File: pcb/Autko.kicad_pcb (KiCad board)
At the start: 2 copper layers, 130 parts, among them J1 PDI, M1 LEFT, M2 RIGHT, Q1 Si4368DY, Q2 BC817, SW2 START, SW3 STOP, U1 LTC3872, U10 CNY70, U11 CNY70, U12 TB6612FNG, U13 RN4678, U2 TLV1117-33, U3 ATxmega16A4U-A, U5 CNY70, U6 CNY70, U7 CNY70, U8 CNY70, U9 CNY70, Y1 8MHz

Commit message: [pcb] Initial layout
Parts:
- removed U13: RN4678, Autko:RN4678
- added REF**: Pololu_ball_caster, Autko:Pololu_ball_caster, F.Cu at (189.7, 48.1)
- added SW1: POWER, Autko:Knitter-Switch_MSS_3112_D, F.Cu at (65.0, 117.5)
- added U4: CNY70, OptoDevice:Vishay_CNY70, F.Cu at (70.6, -19.8)
- R15, R16, R17, R18, R19, R20, R21, R22: value 10kR -> ???R
- U11: value CNY70 -> TB6612FNG; footprint OptoDevice:Vishay_CNY70 -> Package_SO:SSOP-24_5.3x8.2mm_P0.65mm
- U12: value TB6612FNG -> RN4678; footprint Package_SO:SSOP-24_5.3x8.2mm_P0.65mm -> Autko:RN4678
- moved TP14 132.6 mm to (56.0, -6.50)
- moved U11 129.6 mm to (128.5, 176.0), turned to 90 degrees
- moved Y1 119.6 mm to (122.5, 38.5), turned to 180 degrees
- moved R37 119.5 mm to (60.0, -6.50)
- moved Q2 116.7 mm to (65.0, -6.50)
- moved SW2 116.6 mm to (52.8, 84.2)
- moved SW3 115.6 mm to (52.8, 95.2)
- moved C19 114.8 mm to (120.0, 44.5), turned to 180 degrees
- moved M1 114.4 mm to (39.5, 140.5), turned to 90 degrees
- moved C21 109.6 mm to (128.5, 169.5)
- moved TP7 108.7 mm to (72.0, -11.5)
- moved R23 108.3 mm to (70.0, -25.5)
- moved C17 108.0 mm to (64.1, 88.5)
- moved C22 107.9 mm to (122.5, 173.5), turned to -90 degrees
- moved M2 106.6 mm to (159.5, 140.5), turned to -90 degrees
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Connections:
- D10 pad 2: Net-(D10-A) -> /Microcontroller/LED7
- D11 pad 2: Net-(D11-A) -> /Microcontroller/LED8
- D4 pad 2: Net-(D4-A) -> /Microcontroller/LED1
- D5 pad 2: Net-(D5-A) -> /Microcontroller/LED2
- D6 pad 2: Net-(D6-A) -> /Microcontroller/LED3
- D7 pad 2: Net-(D7-A) -> /Microcontroller/LED4
- D8 pad 2: Net-(D8-A) -> /Microcontroller/LED5
- D9 pad 2: Net-(D9-A) -> /Microcontroller/LED6
- R13 pad 2: Net-(U3-AREFA/PA0) -> Net-(U3-PA7)
- R14 pad 1: Net-(U3-AREFA/PA0) -> Net-(U3-PA7)
- R15 pad 1: +3.3V -> Net-(D4-K)
- R15 pad 2: Net-(D4-A) -> GND
- R16 pad 1: +3.3V -> Net-(D5-K)
- R16 pad 2: Net-(D5-A) -> GND
- R17 pad 1: +3.3V -> Net-(D6-K)
- R17 pad 2: Net-(D6-A) -> GND
- R18 pad 1: +3.3V -> Net-(D7-K)
- R18 pad 2: Net-(D7-A) -> GND
- R19 pad 1: +3.3V -> Net-(D8-K)
- R19 pad 2: Net-(D8-A) -> GND
- R20 pad 1: +3.3V -> Net-(D9-K)
- R20 pad 2: Net-(D9-A) -> GND
- R21 pad 1: +3.3V -> Net-(D10-K)
- R21 pad 2: Net-(D10-A) -> GND
- R22 pad 1: +3.3V -> Net-(D11-K)
- R22 pad 2: Net-(D11-A) -> GND
- R23 pad 2: Net-(U5-A) -> Net-(U4-A)
- R25 pad 2: Net-(U6-A) -> Net-(U5-A)
- R27 pad 2: Net-(U7-A) -> Net-(U6-A)
- R29 pad 2: Net-(U8-A) -> Net-(U7-A)
- R31 pad 2: Net-(U9-A) -> Net-(U8-A)
- R33 pad 2: Net-(U10-A) -> Net-(U9-A)
- R35 pad 2: Net-(U11-A) -> Net-(U10-A)
- U10 pad 3: /Line sensors/SENSOR6 -> /Line sensors/SENSOR7
- U11 pad 1: Net-(U11-A) -> Net-(M1-+)
- U11 pad 2: Net-(Q2-C) -> Net-(M1-+)
- U11 pad 3: /Line sensors/SENSOR7 -> GND
- U12 pad 1: Net-(M1-+) -> GND
- U12 pad 10: GND -> unconnected-(U12-PMULDO_O-Pad10)
- U12 pad 11: Net-(M2-+) -> unconnected-(U12-P0_4-Pad11)
- U12 pad 12: Net-(M2-+) -> unconnected-(U12-P1_5-Pad12)
- U12 pad 13: +7.5V -> unconnected-(U12-P1_2-Pad13)
- U12 pad 14: +7.5V -> unconnected-(U12-P1_3-Pad14)
- U12 pad 15: /Microcontroller/M2_PWM -> Net-(JP8-A)
- U12 pad 16: /Microcontroller/M2_IN2 -> /Bluetooth/P0_5
- U12 pad 17: /Microcontroller/M2_IN1 -> Net-(JP7-A)
- U12 pad 18: GND -> /Bluetooth/P2_0
- U12 pad 19: +3.3V -> /Bluetooth/P2_4
- U12 pad 2: Net-(M1-+) -> GND
- U12 pad 20: +3.3V -> /Bluetooth/EAN
- U12 pad 21: /Microcontroller/M1_IN1 -> /Bluetooth/~{RST}
- U12 pad 22: /Microcontroller/M1_IN2 -> Net-(JP6-A)
- U12 pad 23: /Microcontroller/M1_PWM -> Net-(JP5-A)
- U12 pad 24: +7.5V -> unconnected-(U12-P3_1-Pad24)
- U12 pad 4: GND -> +3.3V
- U12 pad 5: Net-(M1--) -> +3.3V
- U12 pad 6: Net-(M1--) -> /Bluetooth/BT_3V3
- U12 pad 7: Net-(M2--) -> /Bluetooth/BT_3V3
- U12 pad 8: Net-(M2--) -> unconnected-(U12-LDO18_O-Pad8)
- U12 pad 9: GND -> unconnected-(U12-WAKEUP-Pad9)
- U3 pad 1: /Line sensors/SENSOR5 -> /Line sensors/SENSOR2
- U3 pad 2: /Line sensors/SENSOR6 -> /Line sensors/SENSOR1
- U3 pad 3: /Line sensors/SENSOR7 -> Net-(U3-PA7)
- U3 pad 40: Net-(U3-AREFA/PA0) -> /Line sensors/SENSOR7
- U3 pad 41: /Line sensors/SENSOR1 -> /Line sensors/SENSOR6
- U3 pad 42: /Line sensors/SENSOR2 -> /Line sensors/SENSOR5
- U3 pad 43: /Line sensors/SENSOR3 -> /Line sensors/SENSOR4
- U3 pad 44: /Line sensors/SENSOR4 -> /Line sensors/SENSOR3
- U5 pad 3: /Line sensors/SENSOR1 -> /Line sensors/SENSOR2
- U6 pad 3: /Line sensors/SENSOR2 -> /Line sensors/SENSOR3
- U7 pad 3: /Line sensors/SENSOR3 -> /Line sensors/SENSOR4
- U8 pad 3: /Line sensors/SENSOR4 -> /Line sensors/SENSOR5
- U9 pad 3: /Line sensors/SENSOR5 -> /Line sensors/SENSOR6
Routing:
- net GND: track 0.00 -> 44.8 mm, vias 0 -> 7
- net /Microcontroller/LED8: track 0.00 -> 28.9 mm
- net /Microcontroller/LED7: track 0.00 -> 27.2 mm
- net /Microcontroller/LED1: track 0.00 -> 25.5 mm
- net /Microcontroller/LED6: track 0.00 -> 25.5 mm
- net /Microcontroller/LED5: track 0.00 -> 23.8 mm
- net /Microcontroller/LED2: track 0.00 -> 23.7 mm
- net /Microcontroller/LED4: track 0.00 -> 22.3 mm
- net /Microcontroller/LED3: track 0.00 -> 22.0 mm
- net +3.3V: track 0.00 -> 11.4 mm
- net Net-(U3-AVCC): track 0.00 -> 5.57 mm
- net Net-(U3-PA7): track 0.00 -> 4.72 mm
- net Net-(D9-K): track 0.00 -> 1.95 mm
- net Net-(D8-K): track 0.00 -> 1.95 mm
- net Net-(D7-K): track 0.00 -> 1.95 mm
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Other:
- board outline added: 140 x 153 mm

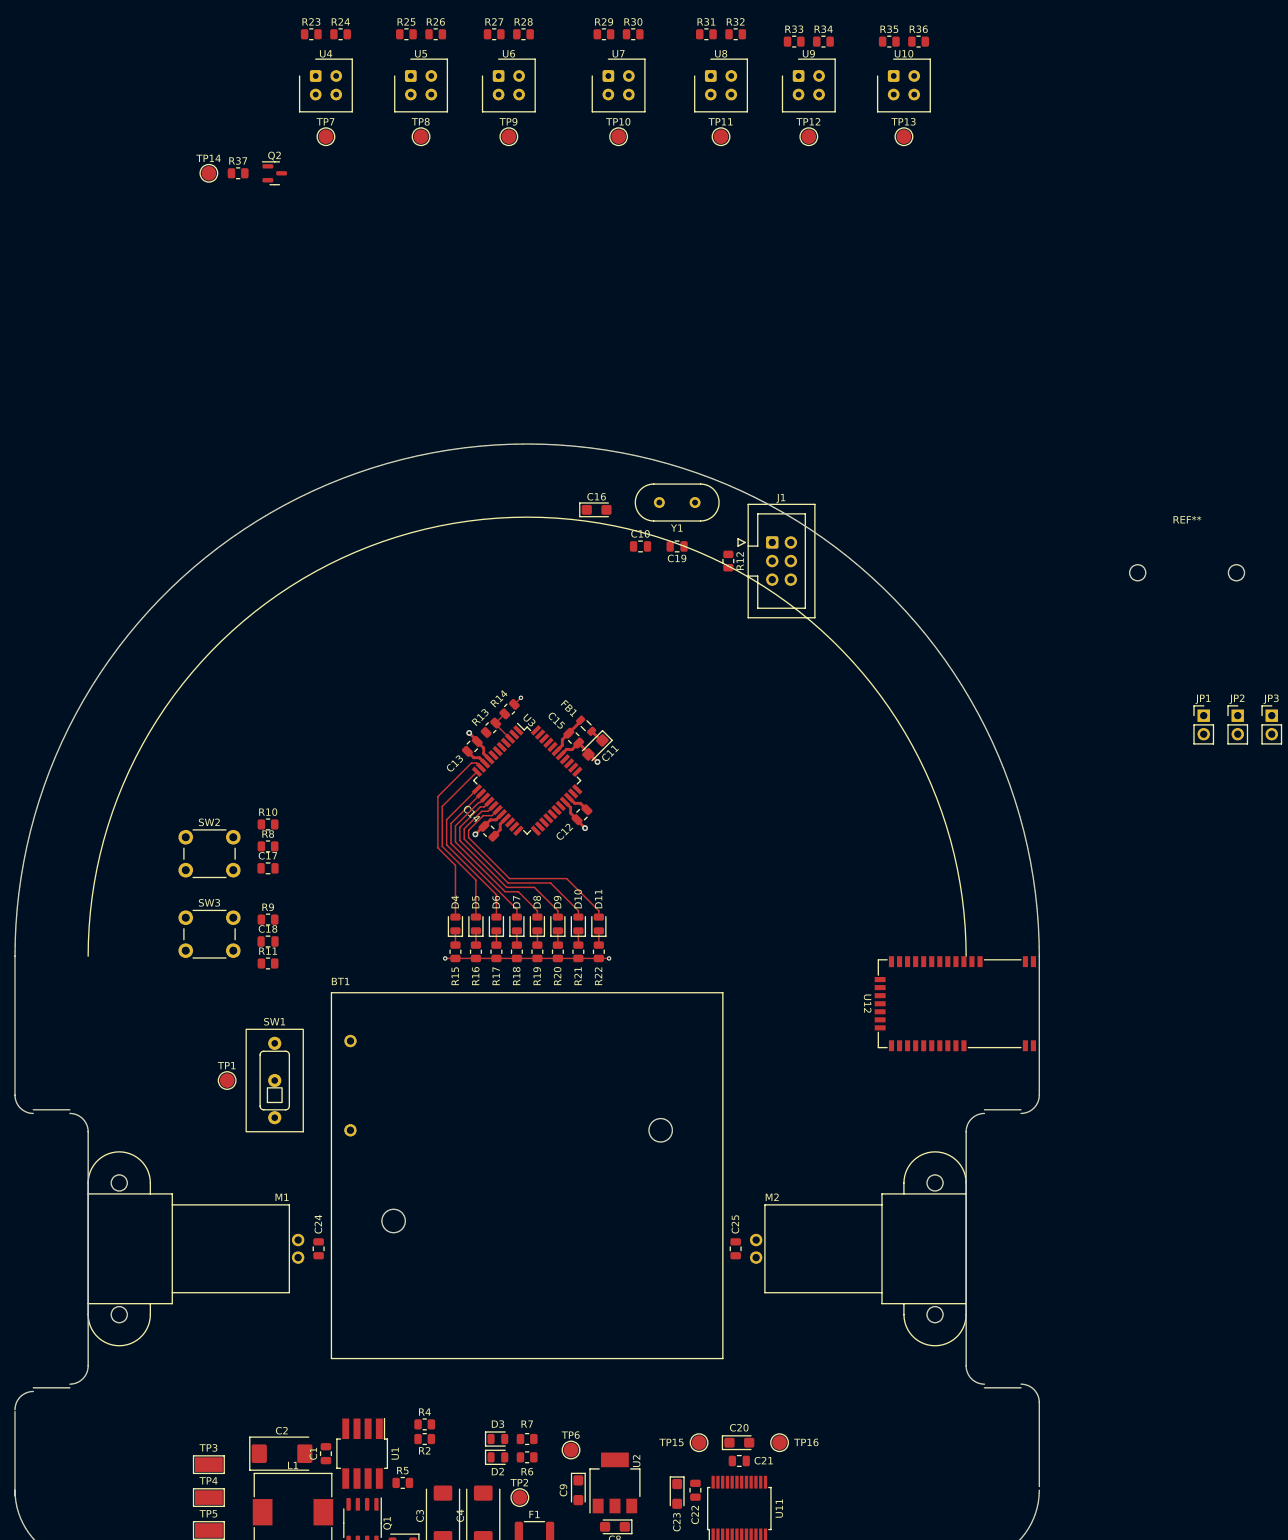
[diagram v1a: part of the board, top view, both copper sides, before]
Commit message: [pcb] Line sensors placed
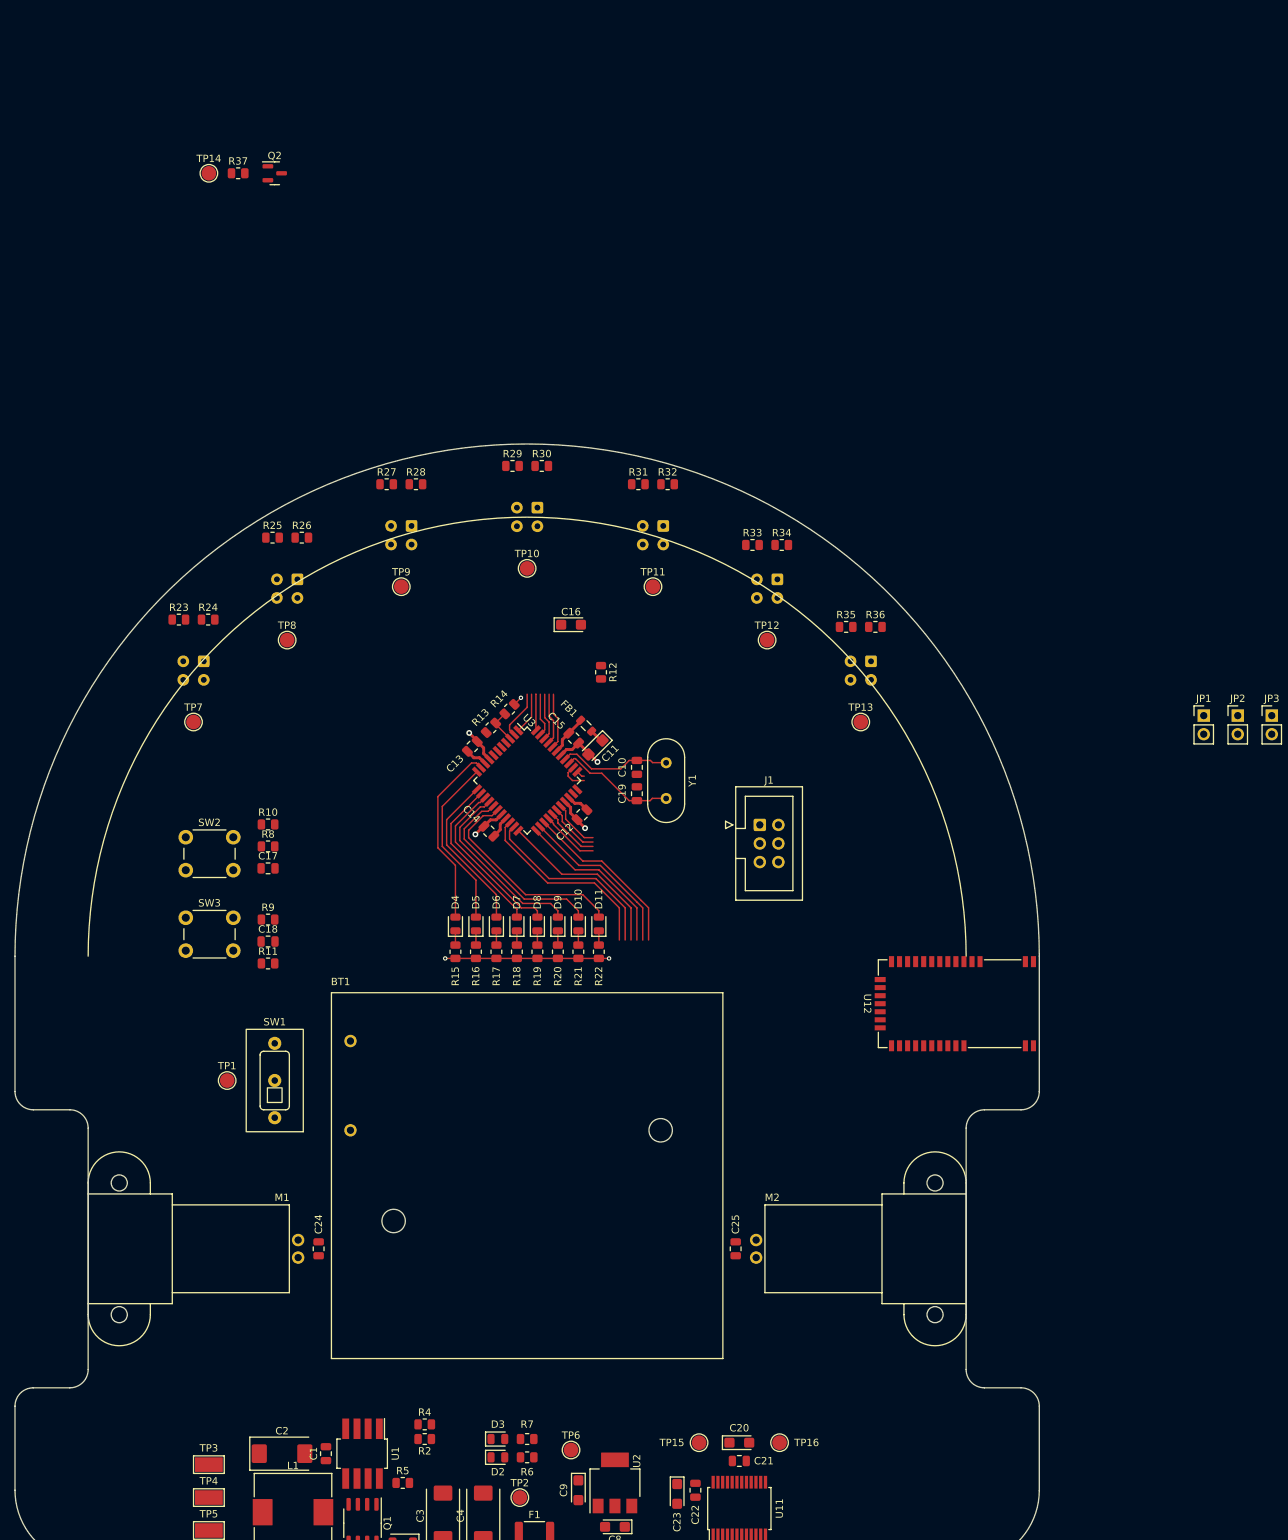
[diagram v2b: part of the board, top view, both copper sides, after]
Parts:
- removed REF**: Pololu_ball_caster, Autko:Pololu_ball_caster
- U10, U4, U5, U6, U7, U8, U9: moved to B.Cu
- moved R23 82.0 mm to (51.9, 54.5)
- moved R24 82.0 mm to (55.9, 54.5)
- moved TP7 82.0 mm to (53.9, 68.5)
- moved U4 81.4 mm to (55.3, 60.2), turned to 180 degrees
- moved R35 80.2 mm to (143.1, 55.5)
- moved R36 80.2 mm to (147.1, 55.5)
- moved TP13 80.2 mm to (145.1, 68.5)
- moved U10 80.1 mm to (146.5, 60.2), turned to 180 degrees
- moved R25 71.2 mm to (64.7, 43.3)
- moved R26 71.2 mm to (68.7, 43.3)
- moved TP8 71.2 mm to (66.7, 57.3)
- moved U5 70.5 mm to (68.1, 49.0), turned to 180 degrees
- moved R33 69.0 mm to (130.3, 44.3)
- moved R34 69.0 mm to (134.3, 44.3)
- moved TP12 69.0 mm to (132.3, 57.3)
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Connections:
- U3 pad 21: /Microcontroller/M1_IN1 -> /Microcontroller/M1_IN2
- U3 pad 22: /Microcontroller/M1_IN2 -> /Microcontroller/M1_IN1
- U3 pad 26: unconnected-(U3-PD6-Pad26) -> /Bluetooth/TX
- U3 pad 27: unconnected-(U3-PD7-Pad27) -> /Bluetooth/RX
- U3 pad 32: /Bluetooth/TX -> unconnected-(U3-PE2-Pad32)
- U3 pad 33: /Bluetooth/RX -> unconnected-(U3-PE3-Pad33)
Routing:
- net /Microcontroller/M1_PWM: track 0.00 -> 26.6 mm
- net /Microcontroller/M1_IN2: track 0.00 -> 26.1 mm
- net /Microcontroller/M1_IN1: track 0.00 -> 24.2 mm
- net /Microcontroller/M2_PWM: track 0.00 -> 23.5 mm
- net /Microcontroller/M2_IN2: track 0.00 -> 23.0 mm
- net /Microcontroller/M2_IN1: track 0.00 -> 22.6 mm
- net /Microcontroller/XTAL2: track 0.00 -> 16.1 mm
- net /Microcontroller/XTAL1: track 0.00 -> 15.6 mm
- net /Bluetooth/TX: track 0.00 -> 8.02 mm
- net /Line sensors/SENSOR7: track 0.00 -> 7.76 mm
- net /Bluetooth/RX: track 0.00 -> 7.63 mm
- net /Bluetooth/RTS: track 0.00 -> 7.25 mm
- net /Line sensors/SENSOR6: track 0.00 -> 7.18 mm
- net /Bluetooth/CTS: track 0.00 -> 6.86 mm
- net /Line sensors/SENSOR1: track 0.00 -> 6.76 mm
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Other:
- outline, holes or cut-outs redrawn
